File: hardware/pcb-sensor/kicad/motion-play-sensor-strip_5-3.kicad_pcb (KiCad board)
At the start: 4 copper layers, 27.3 x 19.1 mm, 34 parts, among them IC1 VCNL4040M3OE, IC2 VCNL4040M3OE, J1 Conn_01x05, U1 PCA9546APWR

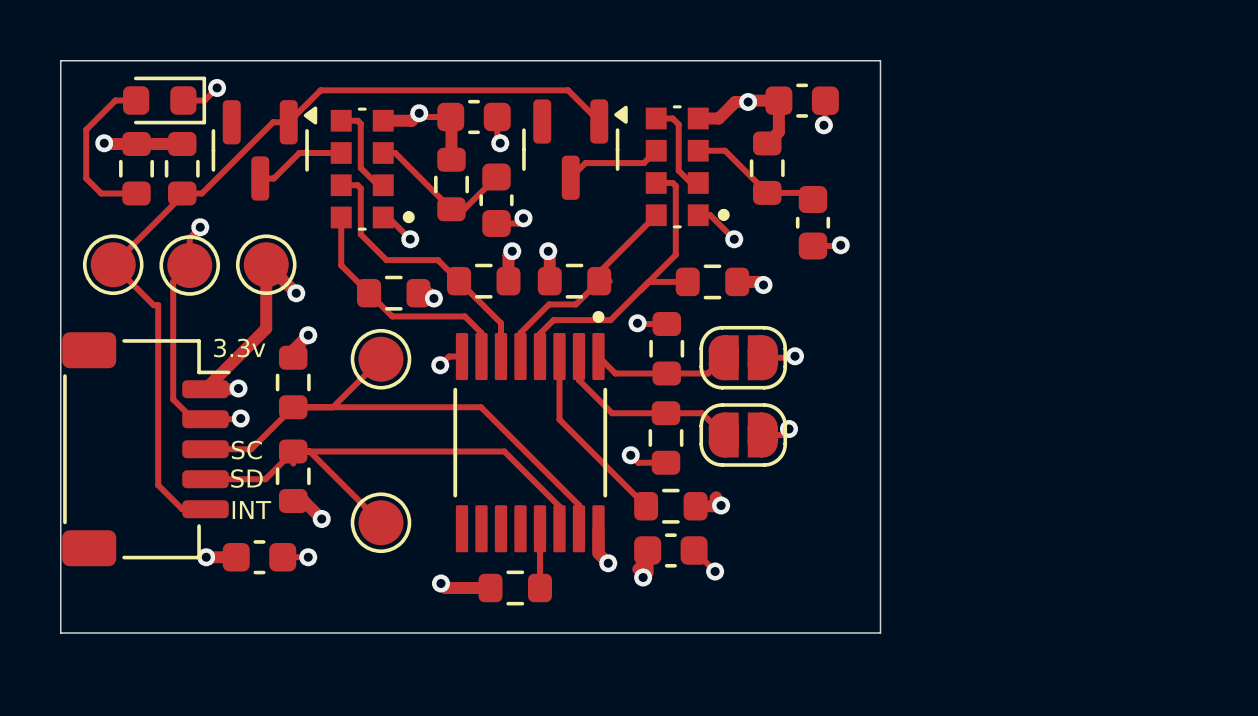
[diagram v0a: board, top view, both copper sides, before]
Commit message: Proximity detection and updated pcbs
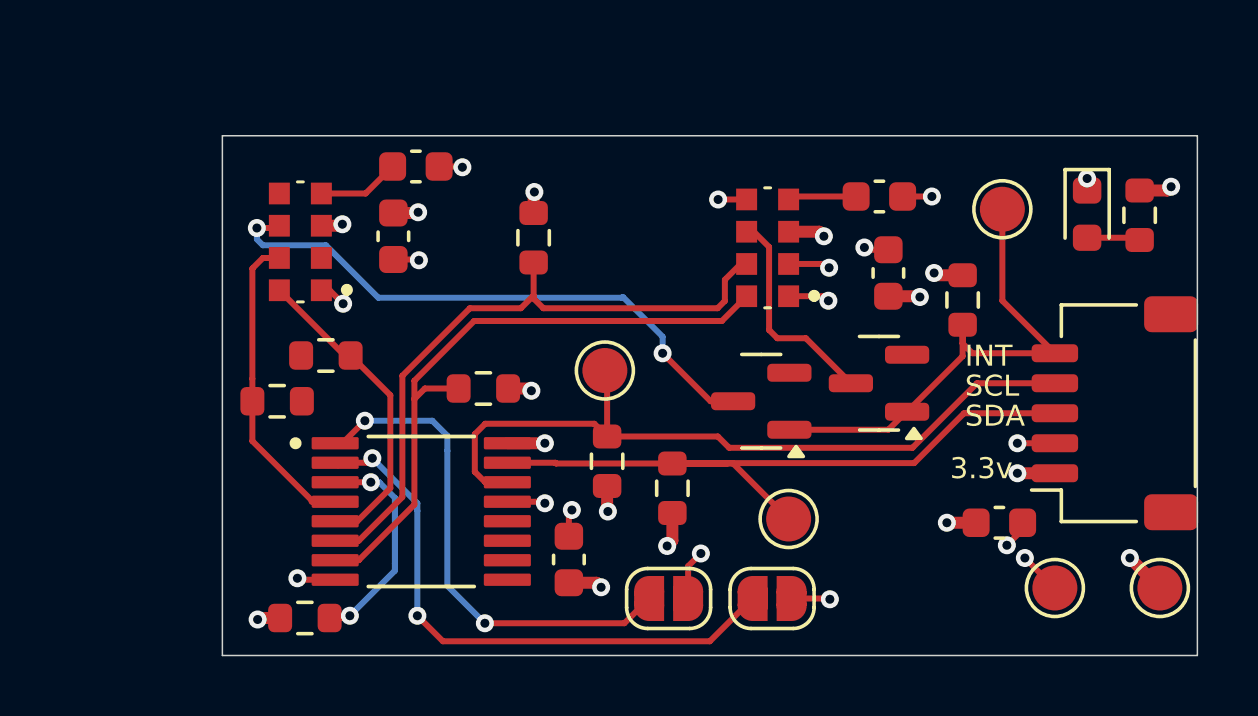
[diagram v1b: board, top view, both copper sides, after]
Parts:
- removed R10, R11: 22Ω, Resistor_SMD:R_0603_1608Metric
- removed R12, R13, R14: 10kΩ, Resistor_SMD:R_0603_1608Metric
- R5: value 8.2kΩ -> 10kΩ
- moved R4 33.5 mm to (172.8, 50.9)
- moved J1 32.3 mm to (172.0, 57.5), turned to 90 degrees
- moved TP1 31.7 mm to (173.5, 63.3)
- moved D1 31.1 mm to (171.1, 50.9), turned to -90 degrees
- moved TP2 30.8 mm to (170.0, 63.3)
- moved TP5 29.7 mm to (168.2, 50.7)
- moved R5 26.4 mm to (166.9, 53.7)
- moved C1 24.7 mm to (168.2, 61.1)
- moved D3 22.0 mm to (164.1, 56.5), turned to 180 degrees
- moved R8 15.0 mm to (144.1, 57.1)
- moved TP3 14.6 mm to (161.1, 61.0), turned to 90 degrees
- moved C7 14.0 mm to (147.9, 51.6)
- moved C4 13.8 mm to (164.2, 50.3)
- moved IC2 13.8 mm to (160.4, 52.0)
- moved C6 13.3 mm to (164.4, 52.8), turned to 90 degrees
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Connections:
- C4 pad 2: +3.3V -> Net-(IC2-A)
- C6 pad 1: Net-(IC2-VDD) -> +3.3V
- C7 pad 1: Net-(IC1-VDD) -> +3.3V
- C8 pad 2: +3.3V -> Net-(IC1-A)
- IC1 pad 2: Net-(IC1-K(LED)) -> GND
- IC1 pad 3: Net-(IC1-VDD) -> +3.3V
- IC1 pad 4: +3.3V -> Net-(IC1-A)
- IC1 pad 5: Net-(IC1-K(LED)) -> GND
- IC2 pad 2: Net-(IC2-K(LED)) -> GND
- IC2 pad 3: Net-(IC2-VDD) -> +3.3V
- IC2 pad 4: +3.3V -> Net-(IC2-A)
- IC2 pad 5: Net-(IC2-K(LED)) -> GND
- JP3 pad 2: +3.3V -> GND
- JP4 pad 2: +3.3V -> GND
- U1 pad 13: Net-(U1-A2) -> GND
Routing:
- net Net-(D2-COM): track 3.22 -> 19.6 mm, vias 0 -> 2
- net +3.3V: track 32.1 -> 16.3 mm, vias 18 -> 16
- net Net-(IC2-SCLK): track 7.99 -> 21.4 mm
- net Net-(JP3-A): track 6.37 -> 19.4 mm, vias 0 -> 2
- net Net-(IC2-SDAT): track 9.24 -> 21.8 mm
- net Net-(JP4-A): track 4.70 -> 16.8 mm, vias 0 -> 2
- net Net-(D2-A): track 29.0 -> 17.2 mm
- net Net-(J1-Pin_4): track 18.0 -> 25.4 mm
- net Net-(IC2-VDD): track 5.00 -> 0.00 mm
- net Net-(J1-Pin_3): track 19.2 -> 24.0 mm
- net Net-(IC1-VDD): track 4.50 -> 0.00 mm
- net Net-(D3-COM): track 3.05 -> 7.19 mm
- net Net-(D1-A): track 5.57 -> 1.78 mm
- net Net-(IC1-K(LED)): track 3.19 -> 0.00 mm
- net Net-(IC2-K(LED)): track 3.15 -> 0.00 mm
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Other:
- board size 27.3 x 19.1 mm -> 32.5 x 17.3 mm
- board text added: "SCL"
- board text added: "SDA"
- board text removed: "SC"
- board text removed: "SD"
